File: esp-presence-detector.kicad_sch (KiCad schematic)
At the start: 8 parts, among them J1 3-pin female, J2 2-pin female, P1 3-pin cable plug, P2 2-pin cable plug, U1 Wemos NodeMCU, U2 AM312

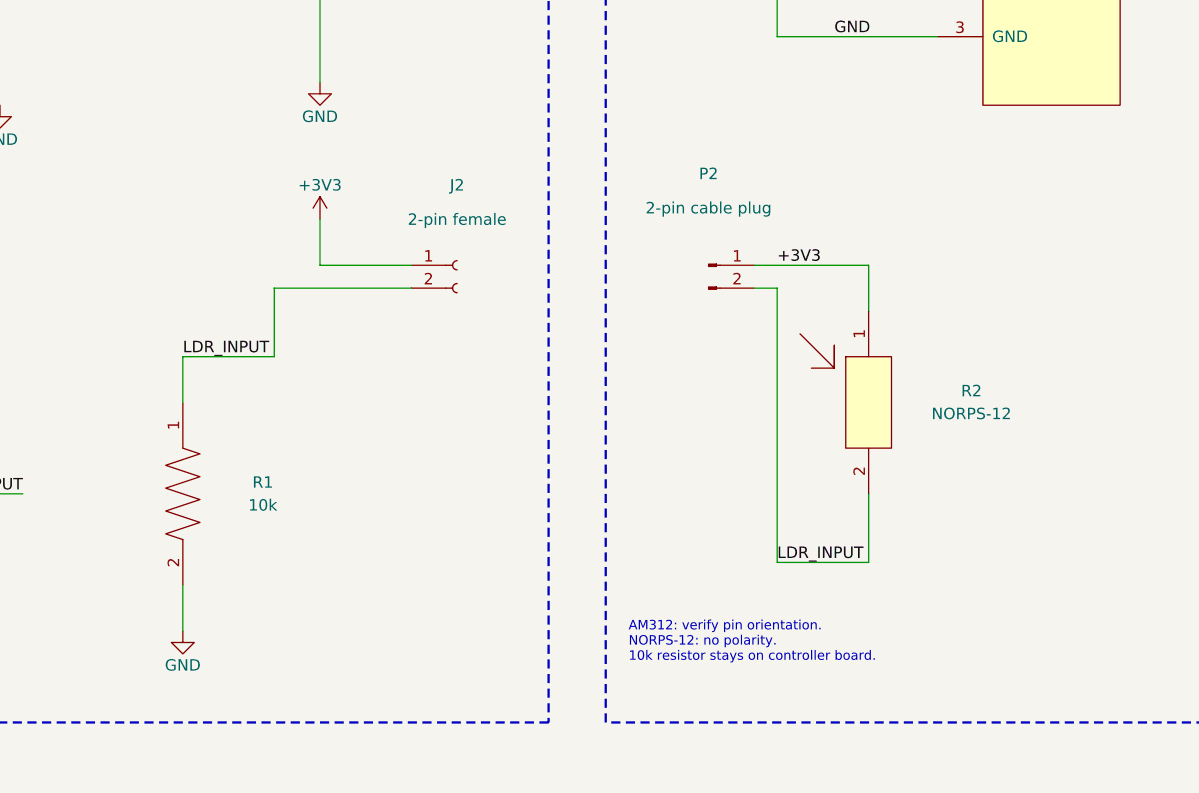
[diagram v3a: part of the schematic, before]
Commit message: fix: erc errors
Ignored a couple of errors to do with the schematic pinouts and parts and then fixed some missing symbols that the AI used weirdly
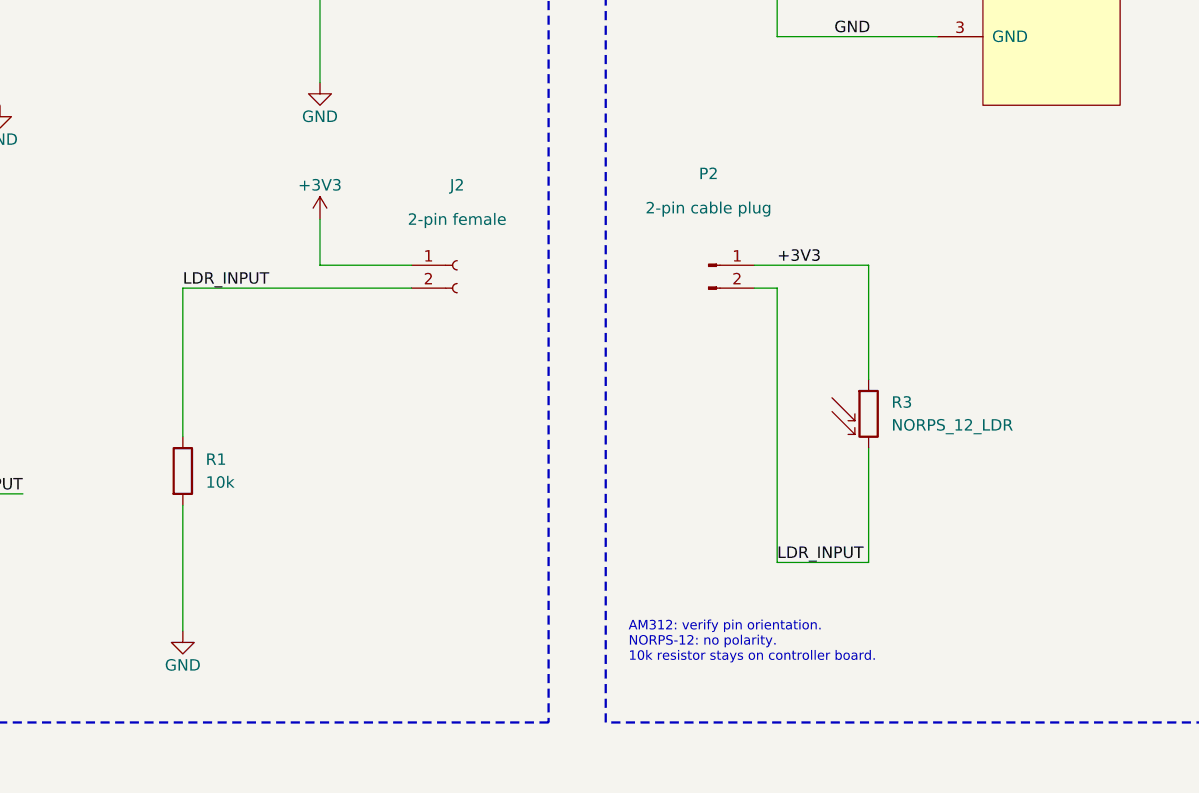
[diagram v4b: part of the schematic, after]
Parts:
- removed R1: 10k, symbol R
- removed R2: NORPS-12, symbol NORPS-12
- added R1: 10k, symbol Device:R
- added R3: NORPS_12_LDR, symbol Device:R_Photo
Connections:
- net +3V3: now also R3.1
- net GND: now also R1.2
- net LDR_INPUT: now also R1.1, R3.2
